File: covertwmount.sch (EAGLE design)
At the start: 56 parts, among them J1 B2B-PH-K-S(LF)(SN), U1 STM32G081RBT6, U2 MMBT4401-7-F

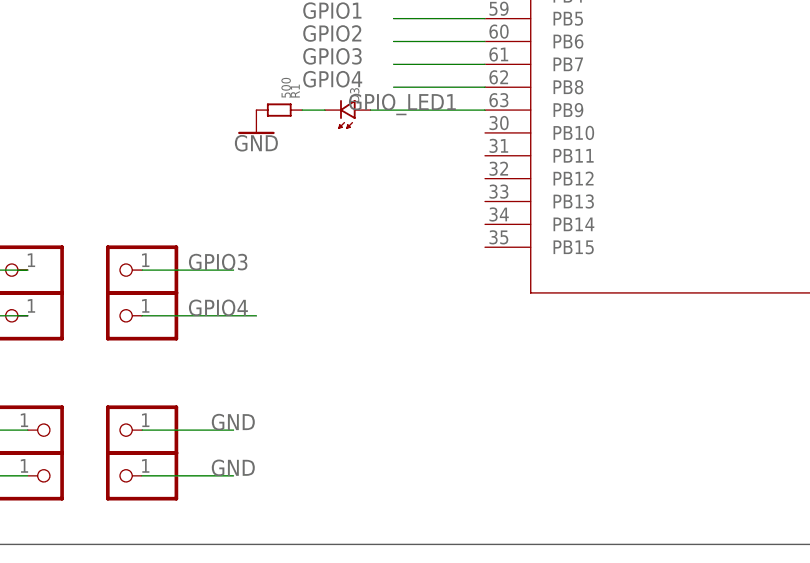
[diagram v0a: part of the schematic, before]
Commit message: pairing button
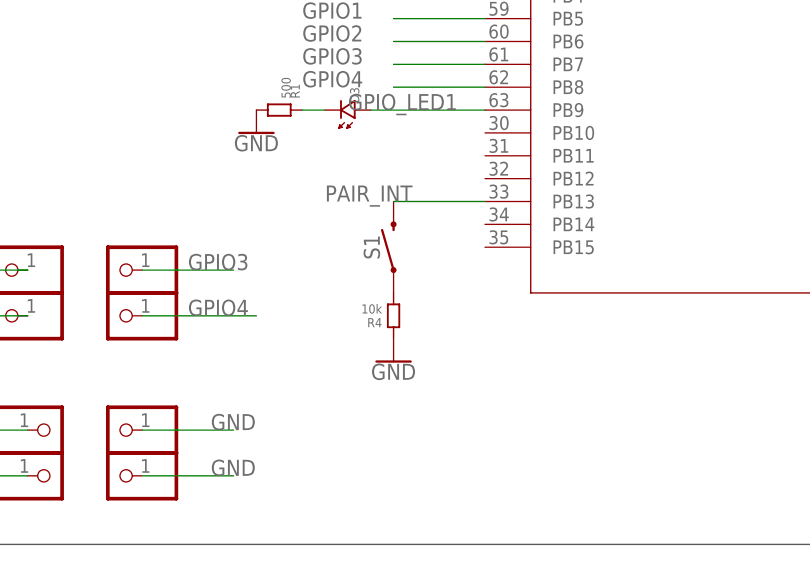
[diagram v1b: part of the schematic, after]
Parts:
- added R4: 10k, standardparts:RESISTOR.0805
- added S1: MOMENTARY-SWITCH-SPST-PTH-6.0MM, SparkFun-Switches:MOMENTARY-SWITCH-SPST-PTH-6.0MM
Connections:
- new net N$9: R4.2, S1.1
- new net PAIR_INT: S1.2, U1.PB13
- net GND: now also R4.1
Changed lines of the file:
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@@
 <part name="R1" library="standardparts" deviceset="RESISTOR" device=".0805" value="500"/>
 <part name="GND10" library="SparkFun-PowerSymbols" library_urn="urn:adsk.eagle:library:530" deviceset="GND" device=""/>
+<part name="S1" library="SparkFun-Switches" library_urn="urn:adsk.eagle:library:535" deviceset="MOMENTARY-SWITCH-SPST" device="-PTH-6.0MM" package3d_urn="urn:adsk.eagle:package:40163/1"/>
+<part name="R4" library="standardparts" deviceset="RESISTOR" device=".0805" value="10k"/>
+<part name="GND11" library="SparkFun-PowerSymbols" library_urn="urn:adsk.eagle:library:530" deviceset="GND" device=""/>
 </parts>
 <sheets>
@@
 <attribute name="VALUE" x="-58.42" y="-51.054" size="1.778" layer="96" align="top-center"/>
 </instance>
+<instance part="S1" gate="G$1" x="-43.18" y="-63.5" smashed="yes" rot="R90">
+<attribute name="NAME" x="-44.704" y="-63.5" size="1.778" layer="95" font="vector" rot="R90" align="bottom-center"/>
+</instance>
+<instance part="R4" gate="G$1" x="-43.18" y="-71.12" smashed="yes" rot="R90">
+<attribute name="NAME" x="-44.45" y="-72.39" size="1.016" layer="95" rot="MR0"/>
+<attribute name="VALUE" x="-44.45" y="-69.85" size="1.016" layer="96" rot="R180"/>
+</instance>
+<instance part="GND11" gate="1" x="-43.18" y="-76.2" smashed="yes">
+<attribute name="VALUE" x="-43.18" y="-76.454" size="1.778" layer="96" align="top-center"/>
+</instance>
 </instances>
 <busses>
@@
 <pinref part="GND10" gate="1" pin="GND"/>
 </segment>
+<segment>
+<pinref part="R4" gate="G$1" pin="1"/>
+<pinref part="GND11" gate="1" pin="GND"/>
+</segment>
 </net>
 <net name="SPI_SCK" class="0">
@@
 </segment>
 </net>
+<net name="PAIR_INT" class="0">
+<segment>
+<pinref part="U1" gate="A" pin="PB13"/>
+<wire x1="-33.02" y1="-58.42" x2="-43.18" y2="-58.42" width="0.1524" layer="91"/>
+<label x="-50.8" y="-58.42" size="1.778" layer="95"/>
+<pinref part="S1" gate="G$1" pin="2"/>
+</segment>
+</net>
+<net name="N$9" class="0">
+<segment>
+<pinref part="S1" gate="G$1" pin="1"/>
+<pinref part="R4" gate="G$1" pin="2"/>
+</segment>
+</net>
